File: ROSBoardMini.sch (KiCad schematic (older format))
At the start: 71 parts, among them J1 Conn_02x20_Odd_Even, J2 Extension0, J3 Extension1, J4 Extension2, J5 PWR, J6 Extension2, U1 P2X8C4M64P, U10 LY68L6400SLIT, U2 W25Q128JVS, U3 PCA9544APW, U4 BME280, U5 ICM-20948, U6 24LC256, U7 AZ1117-1.8, U8 AZ1117-1.2, U9 AZ1117-2.85, Y1 Crystal_GND23

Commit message: Rooting progress
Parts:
- removed D1: D, Diode_SMD:D_0805_2012Metric, symbol Device:D
- C1, C10, C11, C12, C13, C14, C15, C16, C17, C18, C19, C2, C20, C21, C22, C23, C24, C25, C26, C27, C28, C29, C3, C30, C31, C4, C5, C6, C7, C8, C9: symbol Device:C -> ROSBoardMini-rescue:C-Device
- D2, D3: symbol Device:D -> ROSBoardMini-rescue:D-Device
- J1: symbol Connector_Generic:Conn_02x20_Odd_Even -> ROSBoardMini-rescue:Conn_02x20_Odd_Even-Connector_Generic
- J2, J3, J4, J6: symbol Connector:Conn_01x24_Female -> ROSBoardMini-rescue:Conn_01x24_Female-Connector
- J5: symbol Connector:Conn_01x04_Female -> ROSBoardMini-rescue:Conn_01x04_Female-Connector
- R1, R10, R11, R12, R13, R14, R15, R16, R17, R18, R19, R2, R20, R3, R4, R5, R6, R7, R8, R9: symbol Device:R -> ROSBoardMini-rescue:R-Device
- U2: symbol Memory_Flash:W25Q128JVS -> ROSBoardMini-rescue:W25Q128JVS-Memory_Flash
- U3: symbol Interface_Expansion:PCA9544APW -> ROSBoardMini-rescue:PCA9544APW-Interface_Expansion
- U4: symbol Sensor:BME280 -> ROSBoardMini-rescue:BME280-Sensor
- U5: symbol Sensor_Motion:ICM-20948 -> ROSBoardMini-rescue:ICM-20948-Sensor_Motion
- U6: symbol Memory_EEPROM:24LC256 -> ROSBoardMini-rescue:24LC256-Memory_EEPROM
- U7: symbol Regulator_Linear:AZ1117-1.8 -> ROSBoardMini-rescue:AZ1117-1.8-Regulator_Linear
- U8: symbol Regulator_Linear:AZ1117-1.2 -> ROSBoardMini-rescue:AZ1117-1.2-Regulator_Linear
- U9: symbol Regulator_Linear:AZ1117-2.85 -> ROSBoardMini-rescue:AZ1117-2.85-Regulator_Linear
- Y1: symbol Device:Crystal_GND23 -> ROSBoardMini-rescue:Crystal_GND23-Device
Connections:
- net +BATT: now also J5.1 (Pin_1); no longer U1.7 (P3)
- net CSI0_HSYNC: now also U1.4 (P1); no longer U1.48 (P30)
- net CSI0_MCLK: now also U1.6 (P2); no longer U1.39 (P24)
- net CSI0_PCLK: now also U1.7 (P3); no longer U1.43 (P27)
- net CSI0_VSYNC: now also U1.3 (P0)
- net CSI1_HSYNC: now also U1.18 (P10)
- net CSI1_MCLK: now also U1.16 (P9); no longer U1.40 (P25)
- net CSI1_PCLK: now also U1.15 (P8); no longer U1.45 (P28)
- net CSI1_VSYNC: now also U1.19 (P11)
- net CSI2_HSYNC: now also U1.12 (P6)
- net CSI2_MCLK: now also U1.10 (P5); no longer U1.42 (P26)
- net CSI2_PCLK: now also U1.9 (P4); no longer U1.46 (P29)
- net CSI2_VSYNC: now also U1.13 (P7)
- net GPIO1: now also J6.8 (Pin_8); no longer J6.6 (Pin_6)
- net GPIO23: now also J6.17 (Pin_17); no longer J6.2 (Pin_2)
- net GPIO24: now also J6.18 (Pin_18); no longer J6.3 (Pin_3)
- net GPIO26: now also J6.16 (Pin_16); no longer J6.1 (Pin_1)
- net GPIO28: now also J6.19 (Pin_19); no longer J6.5 (Pin_5)
- net GPIO29: now also J6.20 (Pin_20); no longer J6.4 (Pin_4)
- net GPIO8: now also J6.6 (Pin_6); no longer J6.8 (Pin_8)
- net I2C_SCL: now also U1.22 (P13)
- net I2C_SDA: now also U1.21 (P12)
- net IO0: now also J6.1 (Pin_1), U1.24 (P14); no longer J6.16 (Pin_16)
- net IO1: now also J6.2 (Pin_2), U1.25 (P15); no longer J6.17 (Pin_17)
- net IO2: now also J6.3 (Pin_3), U1.27 (P16); no longer J6.18 (Pin_18)
- net IO3: now also J6.4 (Pin_4), U1.28 (P17); no longer J6.19 (Pin_19)
- net IO4: now also J6.5 (Pin_5), U1.30 (P18); no longer J6.20 (Pin_20)
- net IO5: now also U1.31 (P19)
- net PSRAM_CE: now also U1.42 (P26)
- net PSRAM_D0: now also U1.48 (P30)
- net PSRAM_D1: now also U1.46 (P29)
- net PSRAM_D2: now also U1.45 (P28)
- net PSRAM_D3: now also U1.43 (P27)
- net PSRAM_SCLK: now also U1.40 (P25)
- net SPI_CS0: no longer U1.9 (P4)
- net SPI_MISO: now also U1.54 (P33); no longer U1.12 (P6)
- net SPI_MOSI: now also U1.53 (P32); no longer U1.10 (P5)
- net SPI_SCK: now also U1.49 (P31); no longer U1.13 (P7)
- no-connect marks 33 -> 34

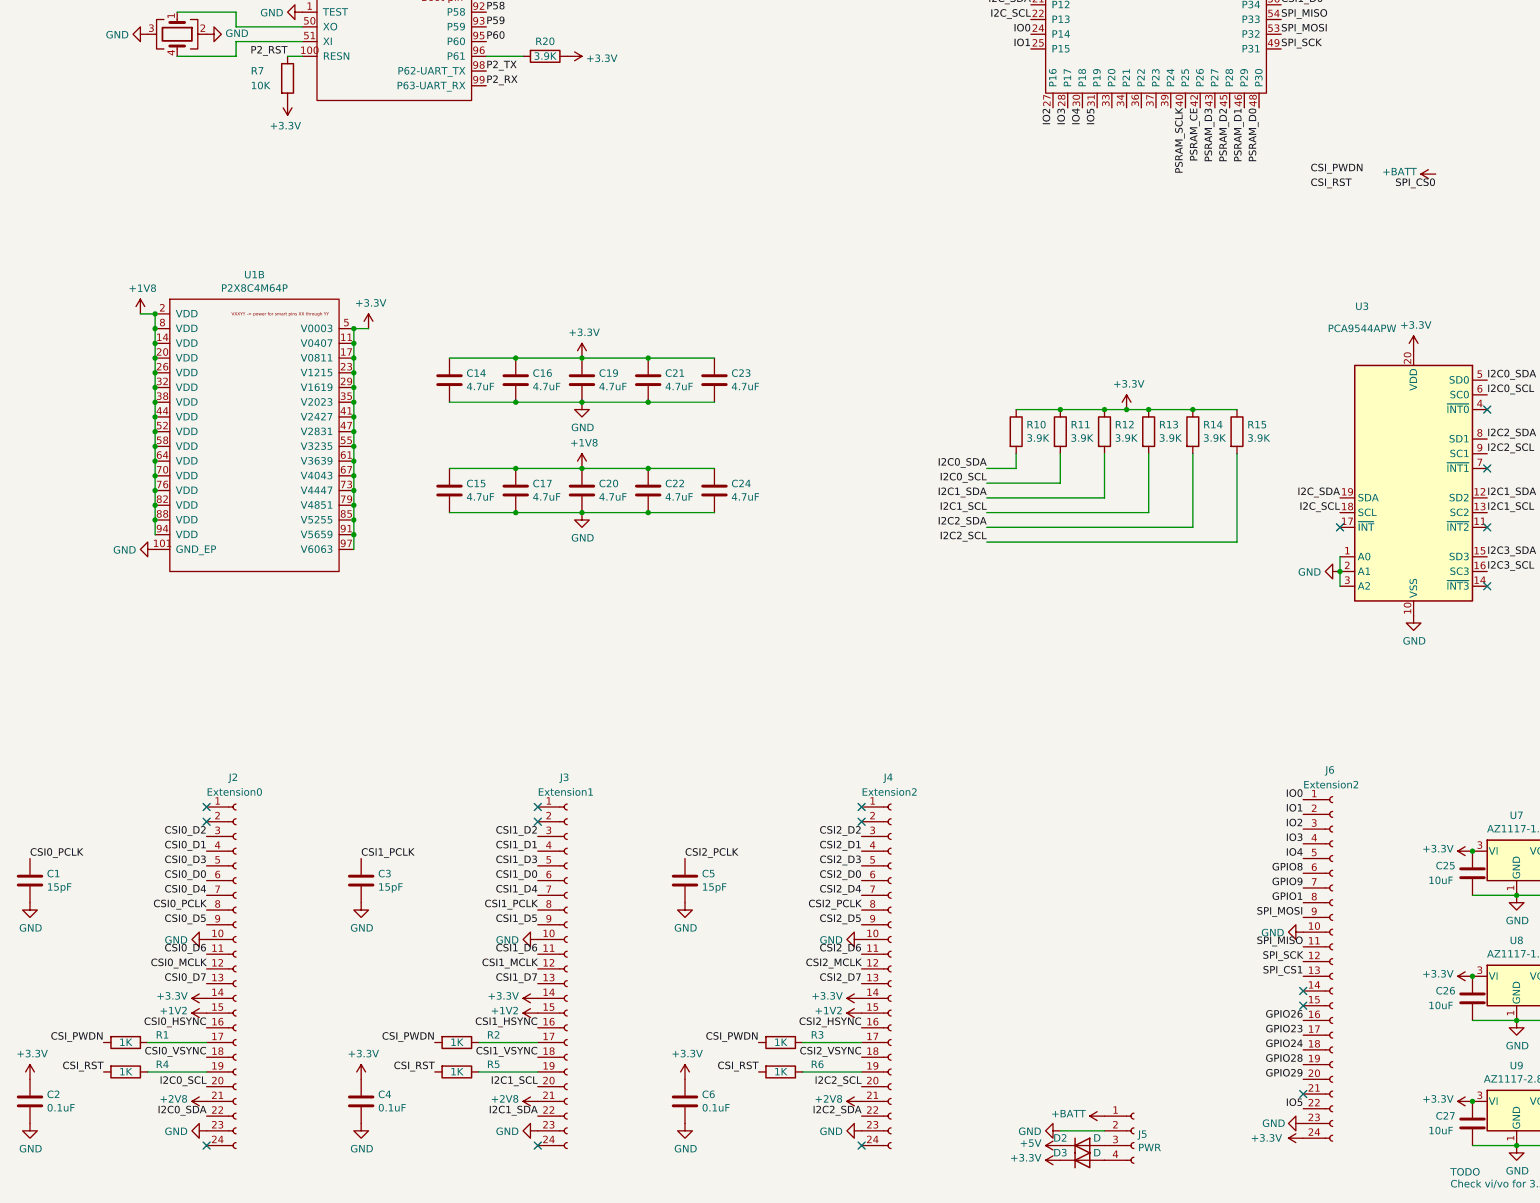
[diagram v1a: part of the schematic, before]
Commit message: Re arrange pin to allow 1 cog to use 3 camera + rooting progress
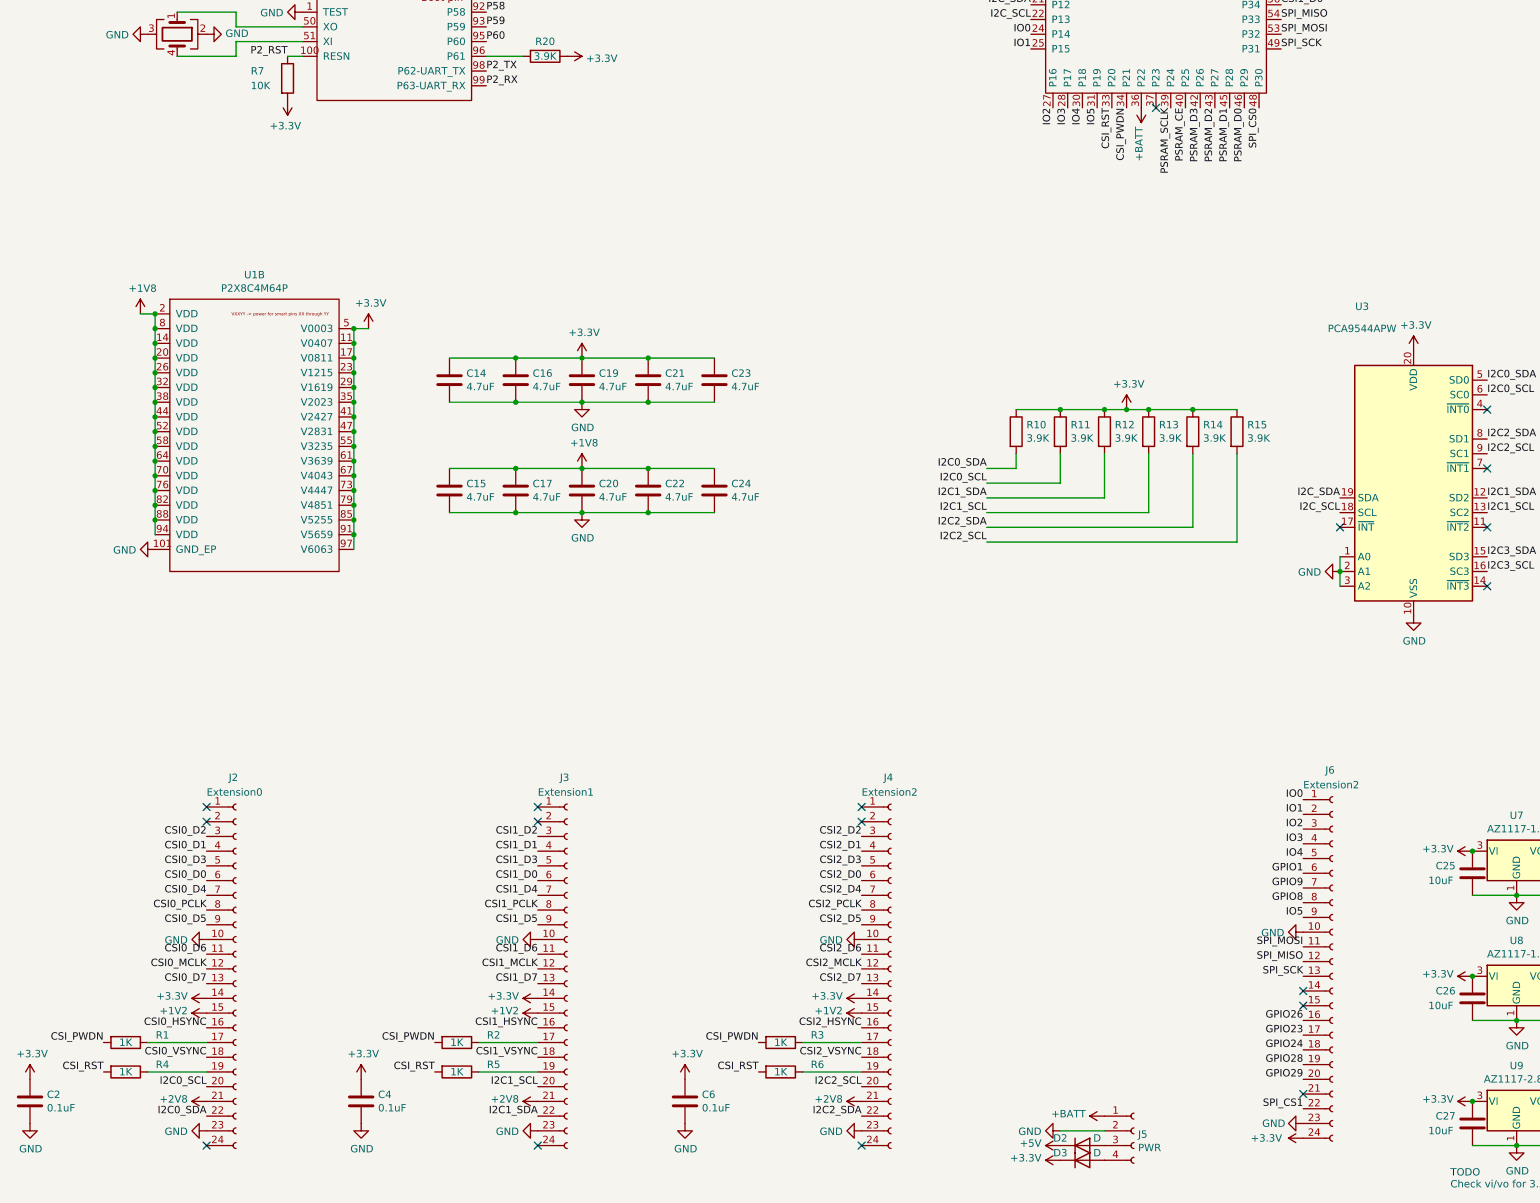
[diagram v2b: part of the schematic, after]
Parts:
- removed C1, C3, C5: 15pF, Capacitor_SMD:C_0402_1005Metric, symbol ROSBoardMini-rescue:C-Device
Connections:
- net +BATT: now also U1.36 (P22)
- net CSI_PWDN: now also U1.34 (P21)
- net CSI_RST: now also U1.33 (P20)
- net GPIO1: now also J6.6 (Pin_6); no longer J6.8 (Pin_8)
- net GPIO8: now also J6.8 (Pin_8); no longer J6.6 (Pin_6)
- net IO5: now also J6.9 (Pin_9); no longer J6.22 (Pin_22)
- net PSRAM_CE: now also U1.40 (P25); no longer U1.42 (P26)
- net PSRAM_D0: now also U1.46 (P29); no longer U1.48 (P30)
- net PSRAM_D1: now also U1.45 (P28); no longer U1.46 (P29)
- net PSRAM_D2: now also U1.43 (P27); no longer U1.45 (P28)
- net PSRAM_D3: now also U1.42 (P26); no longer U1.43 (P27)
- net PSRAM_SCLK: now also U1.39 (P24); no longer U1.40 (P25)
- net SPI_CS0: now also U1.48 (P30)
- net SPI_CS1: now also J6.22 (Pin_22); no longer J6.13 (Pin_13)
- net SPI_MISO: now also J6.12 (Pin_12); no longer J6.11 (Pin_11)
- net SPI_MOSI: now also J6.11 (Pin_11); no longer J6.9 (Pin_9)
- net SPI_SCK: now also J6.13 (Pin_13); no longer J6.12 (Pin_12)
- no-connect marks 34 -> 35
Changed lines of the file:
@@
 CSI0_D7
-$Comp
-L ROSBoardMini-rescue:C-Device C1
-U 1 1 5F9BDA0E
-P 600 9050
-F 0 "C1" H 715 9096 50  0000 L CNN
-F 1 "15pF" H 715 9005 50  0000 L CNN
-F 2 "Capacitor_SMD:C_0402_1005Metric" H 638 8900 50  0001 C CNN
-F 3 "~" H 600 9050 50  0001 C CNN
-	1    600  9050
-	1    0    0    -1
-$EndComp
-$Comp
-L ROSBoardMini-rescue:GND-power #PWR0108
-U 1 1 5F9BE39C
-P 600 9200
-F 0 "#PWR0108" H 600 8950 50  0001 C CNN
-F 1 "GND" H 605 9027 50  0000 C CNN
-F 2 "" H 600 9200 50  0001 C CNN
-F 3 "" H 600 9200 50  0001 C CNN
-	1    600  9200
-	1    0    0    -1
-$EndComp
 $Comp
 L ROSBoardMini-rescue:C-Device C2
@@
 	1    0    0    -1
 $EndComp
-Text Label 600  8900 0    50   ~ 0
-CSI0_PCLK
 NoConn ~ 4050 8650
 NoConn ~ 4050 10850
@@
 CSI1_D7
 $Comp
-L ROSBoardMini-rescue:C-Device C3
-U 1 1 5F9CCF01
-P 2850 9050
-F 0 "C3" H 2965 9096 50  0000 L CNN
-F 1 "15pF" H 2965 9005 50  0000 L CNN
-F 2 "Capacitor_SMD:C_0402_1005Metric" H 2888 8900 50  0001 C CNN
-F 3 "~" H 2850 9050 50  0001 C CNN
-	1    2850 9050
-	1    0    0    -1
-$EndComp
-$Comp
-L ROSBoardMini-rescue:GND-power #PWR0118
-U 1 1 5F9CCF07
-P 2850 9200
-F 0 "#PWR0118" H 2850 8950 50  0001 C CNN
-F 1 "GND" H 2855 9027 50  0000 C CNN
-F 2 "" H 2850 9200 50  0001 C CNN
-F 3 "" H 2850 9200 50  0001 C CNN
-	1    2850 9200
-	1    0    0    -1
-$EndComp
-$Comp
 L ROSBoardMini-rescue:C-Device C4
 U 1 1 5F9CCF0D
@@
 	1    0    0    -1
 $EndComp
-Text Label 2850 8900 0    50   ~ 0
-CSI1_PCLK
 NoConn ~ 6250 8550
 NoConn ~ 6250 8650
@@
 CSI2_D7
 $Comp
-L ROSBoardMini-rescue:C-Device C5
-U 1 1 5F9D705C
-P 5050 9050
-F 0 "C5" H 5165 9096 50  0000 L CNN
-F 1 "15pF" H 5165 9005 50  0000 L CNN
-F 2 "Capacitor_SMD:C_0402_1005Metric" H 5088 8900 50  0001 C CNN
-F 3 "~" H 5050 9050 50  0001 C CNN
-	1    5050 9050
-	1    0    0    -1
-$EndComp
-$Comp
-L ROSBoardMini-rescue:GND-power #PWR0128
-U 1 1 5F9D7062
-P 5050 9200
-F 0 "#PWR0128" H 5050 8950 50  0001 C CNN
-F 1 "GND" H 5055 9027 50  0000 C CNN
-F 2 "" H 5050 9200 50  0001 C CNN
-F 3 "" H 5050 9200 50  0001 C CNN
-	1    5050 9200
-	1    0    0    -1
-$EndComp
-$Comp
 L ROSBoardMini-rescue:C-Device C6
 U 1 1 5F9D7068
@@
 	1    0    0    -1
 $EndComp
-Text Label 5050 8900 0    50   ~ 0
-CSI2_PCLK
 Text Label 8200 1500 1    50   ~ 0
 CSI0_D2
@@
 Text Label 13150 3300 0    50   ~ 0
 SPI_CS1
-Text Label 10150 4350 2    50   ~ 0
+Text Label 8950 3800 3    50   ~ 0
 SPI_CS0
 Text Label 12650 2900 2    50   ~ 0
@@
 L ROSBoardMini-rescue:+BATT-power #PWR0137
 U 1 1 5FA1657C
-P 10150 4250
-F 0 "#PWR0137" H 10150 4100 50  0001 C CNN
-F 1 "+BATT" V 10165 4378 50  0000 L CNN
-F 2 "" H 10150 4250 50  0001 C CNN
-F 3 "" H 10150 4250 50  0001 C CNN
-	1    10150 4250
-	0    -1   -1   0
+P 8150 3800
+F 0 "#PWR0137" H 8150 3650 50  0001 C CNN
+F 1 "+BATT" V 8165 3928 50  0000 L CNN
+F 2 "" H 8150 3800 50  0001 C CNN
+F 3 "" H 8150 3800 50  0001 C CNN
+	1    8150 3800
+	-1   0    0    1
 $EndComp
 Text Label 7850 3800 3    50   ~ 0
@@
 Text Label 7400 3300 2    50   ~ 0
 IO0
-Text Label 9250 10600 2    50   ~ 0
+Text Label 9250 9300 2    50   ~ 0
 IO5
 Text Label 9250 8900 2    50   ~ 0
@@
 Text Label 9250 8500 2    50   ~ 0
 IO0
+Text Label 9250 10600 2    50   ~ 0
+SPI_CS1
+Text Label 9250 9500 2    50   ~ 0
+SPI_MOSI
+Text Label 9250 9600 2    50   ~ 0
+SPI_MISO
 Text Label 9250 9700 2    50   ~ 0
-SPI_CS1
-Text Label 9250 9300 2    50   ~ 0
-SPI_MOSI
-Text Label 9250 9500 2    50   ~ 0
-SPI_MISO
-Text Label 9250 9600 2    50   ~ 0
 SPI_SCK
 Text Label 12650 2200 2    50   ~ 0
@@
 Text Label 12650 2300 2    50   ~ 0
 GPIO9
-Text Label 9250 9000 2    50   ~ 0
+Text Label 9250 9200 2    50   ~ 0
 GPIO8
 Text Label 9250 9100 2    50   ~ 0
@@
 Text Label 13150 2600 0    50   ~ 0
 GPIO1
-Text Label 9250 9200 2    50   ~ 0
+Text Label 9250 9000 2    50   ~ 0
 GPIO1
 Text Label 13150 3900 0    50   ~ 0
@@
 Text Label 2550 1950 0    50   ~ 0
 PSRAM_D3
+Text Label 8450 3800 3    50   ~ 0
+PSRAM_CE
+Text Label 8350 3800 3    50   ~ 0
+PSRAM_SCLK
+Text Label 8850 3800 3    50   ~ 0
+PSRAM_D0
+Text Label 8750 3800 3    50   ~ 0
+PSRAM_D1
 Text Label 8550 3800 3    50   ~ 0
-PSRAM_CE
-Text Label 8450 3800 3    50   ~ 0
-PSRAM_SCLK
-Text Label 8950 3800 3    50   ~ 0
-PSRAM_D0
-Text Label 8850 3800 3    50   ~ 0
-PSRAM_D1
+PSRAM_D3
 Text Label 8650 3800 3    50   ~ 0
-PSRAM_D3
-Text Label 8750 3800 3    50   ~ 0
 PSRAM_D2
 $Comp
@@
 Wire Wire Line
 	4050 10350 3650 10350
-Text Label 9300 4350 0    50   ~ 0
+Text Label 7950 3800 3    50   ~ 0
 CSI_RST
 Text Label 1100 10350 2    50   ~ 0
@@
 Text Label 1100 10150 2    50   ~ 0
 CSI_PWDN
-Text Label 9300 4250 0    50   ~ 0
+Text Label 8050 3800 3    50   ~ 0
 CSI_PWDN
 NoConn ~ 13150 3800
+NoConn ~ 8250 3800
 $EndSCHEMATC

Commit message: Everything rooted except power
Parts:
- removed R1, R2, R3, R4, R5, R6: 1K, Resistor_SMD:R_0201_0603Metric, symbol ROSBoardMini-rescue:R-Device
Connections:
- net CSI_PWDN: now also J2.17 (Pin_17), J3.17 (Pin_17), J4.17 (Pin_17)
- net CSI_RST: now also J2.19 (Pin_19), J3.19 (Pin_19), J4.19 (Pin_19)
- net SPI_MISO: now also J6.11 (Pin_11); no longer J6.12 (Pin_12)
- net SPI_MOSI: now also J6.12 (Pin_12); no longer J6.11 (Pin_11)
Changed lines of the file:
@@
 	0    -1   -1   0
-$EndComp
-$Comp
-L ROSBoardMini-rescue:R-Device R1
-U 1 1 5F9B5B40
-P 1250 10150
-F 0 "R1" V 1200 10400 50  0000 C CNN
-F 1 "1K" V 1250 10150 50  0000 C CNN
-F 2 "Resistor_SMD:R_0201_0603Metric" V 1180 10150 50  0001 C CNN
-F 3 "~" H 1250 10150 50  0001 C CNN
-	1    1250 10150
-	0    1    1    0
 $EndComp
 Text Label 1800 10050 2    50   ~ 0
@@
 Text Label 1800 10250 2    50   ~ 0
 CSI0_VSYNC
-Wire Wire Line
-	1400 10150 1800 10150
 Text Label 1800 10650 2    50   ~ 0
 I2C0_SDA
@@
 	0    -1   -1   0
 $EndComp
-$Comp
-L ROSBoardMini-rescue:R-Device R2
-U 1 1 5F9CCEDD
-P 3500 10150
-F 0 "R2" V 3450 10400 50  0000 C CNN
-F 1 "1K" V 3500 10150 50  0000 C CNN
-F 2 "Resistor_SMD:R_0201_0603Metric" V 3430 10150 50  0001 C CNN
-F 3 "~" H 3500 10150 50  0001 C CNN
-	1    3500 10150
-	0    1    1    0
-$EndComp
 Text Label 4050 10050 2    50   ~ 0
 CSI1_HSYNC
 Text Label 4050 10250 2    50   ~ 0
 CSI1_VSYNC
-Wire Wire Line
-	3650 10150 4050 10150
 Text Label 4050 10650 2    50   ~ 0
 I2C1_SDA
@@
 	0    -1   -1   0
 $EndComp
-$Comp
-L ROSBoardMini-rescue:R-Device R3
-U 1 1 5F9D7038
-P 5700 10150
-F 0 "R3" V 5650 10400 50  0000 C CNN
-F 1 "1K" V 5700 10150 50  0000 C CNN
-F 2 "Resistor_SMD:R_0201_0603Metric" V 5630 10150 50  0001 C CNN
-F 3 "~" H 5700 10150 50  0001 C CNN
-	1    5700 10150
-	0    1    1    0
-$EndComp
 Text Label 6250 10050 2    50   ~ 0
 CSI2_HSYNC
 Text Label 6250 10250 2    50   ~ 0
 CSI2_VSYNC
-Wire Wire Line
-	5850 10150 6250 10150
 Text Label 6250 10650 2    50   ~ 0
 I2C2_SDA
@@
 Text Label 9250 10600 2    50   ~ 0
 SPI_CS1
+Text Label 9250 9600 2    50   ~ 0
+SPI_MOSI
 Text Label 9250 9500 2    50   ~ 0
-SPI_MOSI
-Text Label 9250 9600 2    50   ~ 0
 SPI_MISO
 Text Label 9250 9700 2    50   ~ 0
@@
 	0    1    1    0
 $EndComp
-Text Label 5550 10350 2    50   ~ 0
+Text Label 6250 10350 2    50   ~ 0
 CSI_RST
-$Comp
-L ROSBoardMini-rescue:R-Device R6
-U 1 1 5FBAB627
-P 5700 10350
-F 0 "R6" V 5650 10600 50  0000 C CNN
-F 1 "1K" V 5700 10350 50  0000 C CNN
-F 2 "Resistor_SMD:R_0201_0603Metric" V 5630 10350 50  0001 C CNN
-F 3 "~" H 5700 10350 50  0001 C CNN
-	1    5700 10350
-	0    1    1    0
-$EndComp
-Wire Wire Line
-	6250 10350 5850 10350
-Text Label 3350 10350 2    50   ~ 0
+Text Label 4050 10350 2    50   ~ 0
 CSI_RST
-$Comp
-L ROSBoardMini-rescue:R-Device R5
-U 1 1 5FBC3625
-P 3500 10350
-F 0 "R5" V 3450 10600 50  0000 C CNN
-F 1 "1K" V 3500 10350 50  0000 C CNN
-F 2 "Resistor_SMD:R_0201_0603Metric" V 3430 10350 50  0001 C CNN
-F 3 "~" H 3500 10350 50  0001 C CNN
-	1    3500 10350
-	0    1    1    0
-$EndComp
-Wire Wire Line
-	4050 10350 3650 10350
 Text Label 7950 3800 3    50   ~ 0
 CSI_RST
-Text Label 1100 10350 2    50   ~ 0
+Text Label 1800 10350 2    50   ~ 0
 CSI_RST
-$Comp
-L ROSBoardMini-rescue:R-Device R4
-U 1 1 5FBD8556
-P 1250 10350
-F 0 "R4" V 1200 10600 50  0000 C CNN
-F 1 "1K" V 1250 10350 50  0000 C CNN
-F 2 "Resistor_SMD:R_0201_0603Metric" V 1180 10350 50  0001 C CNN
-F 3 "~" H 1250 10350 50  0001 C CNN
-	1    1250 10350
-	0    1    1    0
-$EndComp
-Wire Wire Line
-	1800 10350 1400 10350
-Text Label 5550 10150 2    50   ~ 0
+Text Label 6250 10150 2    50   ~ 0
 CSI_PWDN
-Text Label 3350 10150 2    50   ~ 0
+Text Label 4050 10150 2    50   ~ 0
 CSI_PWDN
-Text Label 1100 10150 2    50   ~ 0
+Text Label 1800 10150 2    50   ~ 0
 CSI_PWDN
 Text Label 8050 3800 3    50   ~ 0
